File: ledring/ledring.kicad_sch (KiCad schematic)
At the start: 22 parts, among them U1 LM3914V, U2 LM3914V

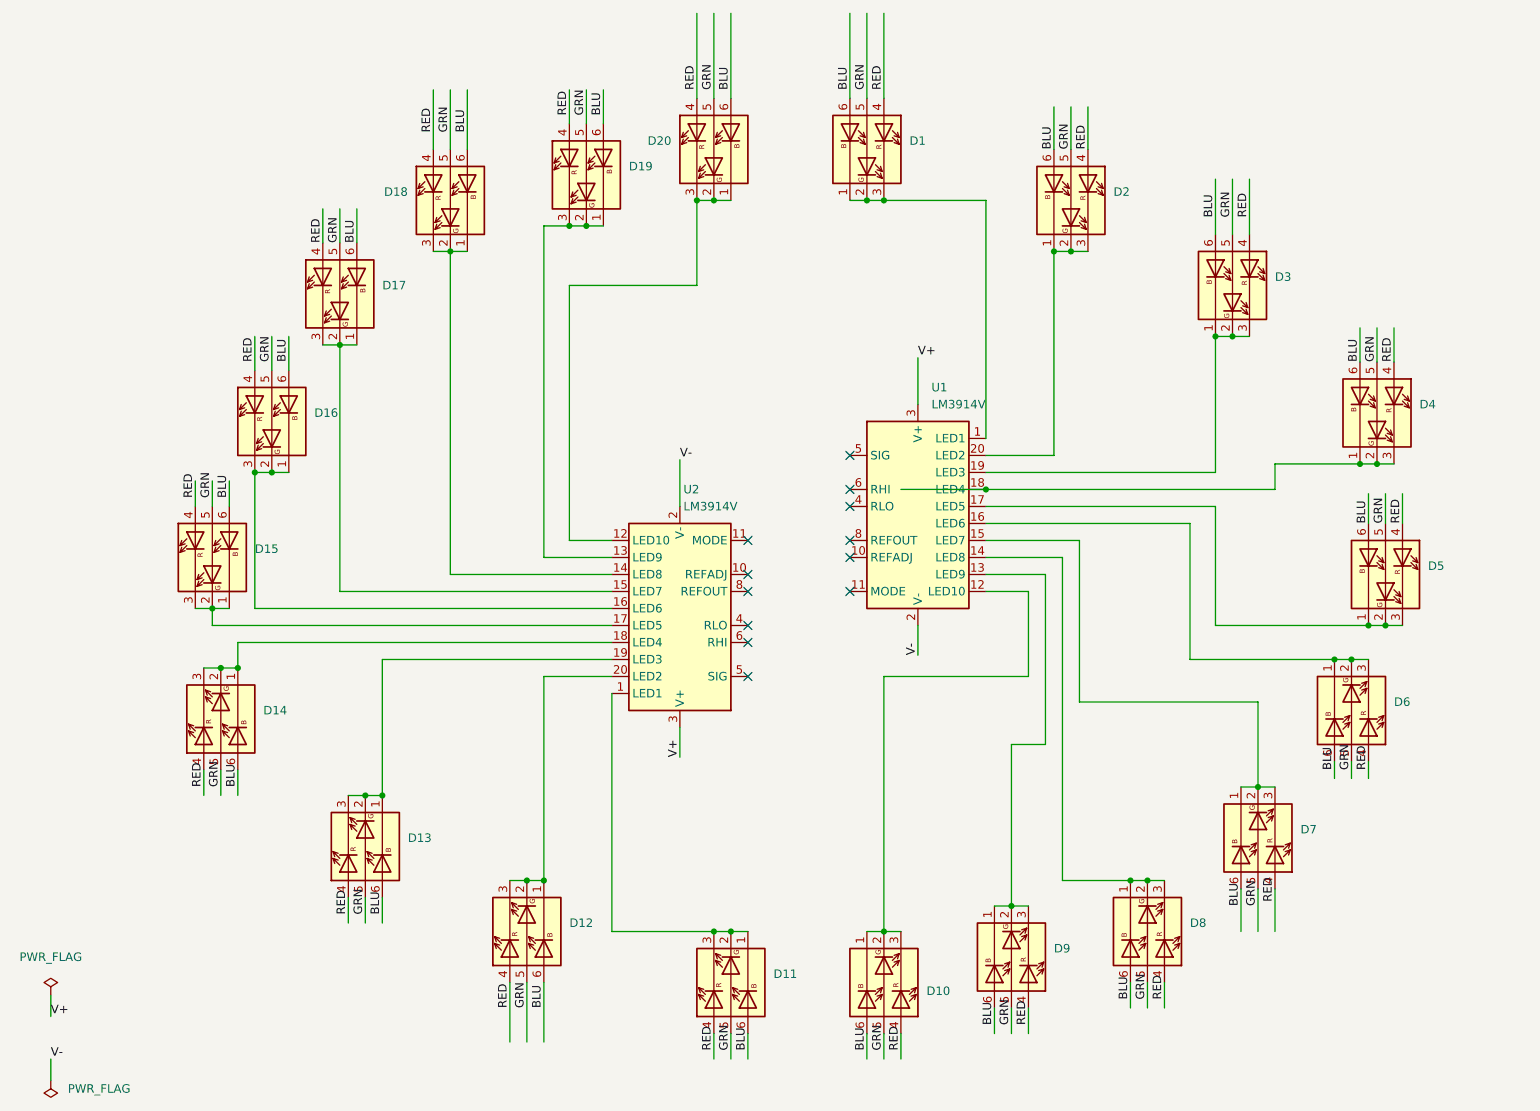
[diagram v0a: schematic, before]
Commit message: ledring: switch from LM3914V (PLCC-20) to LM3914N (DIP-18)
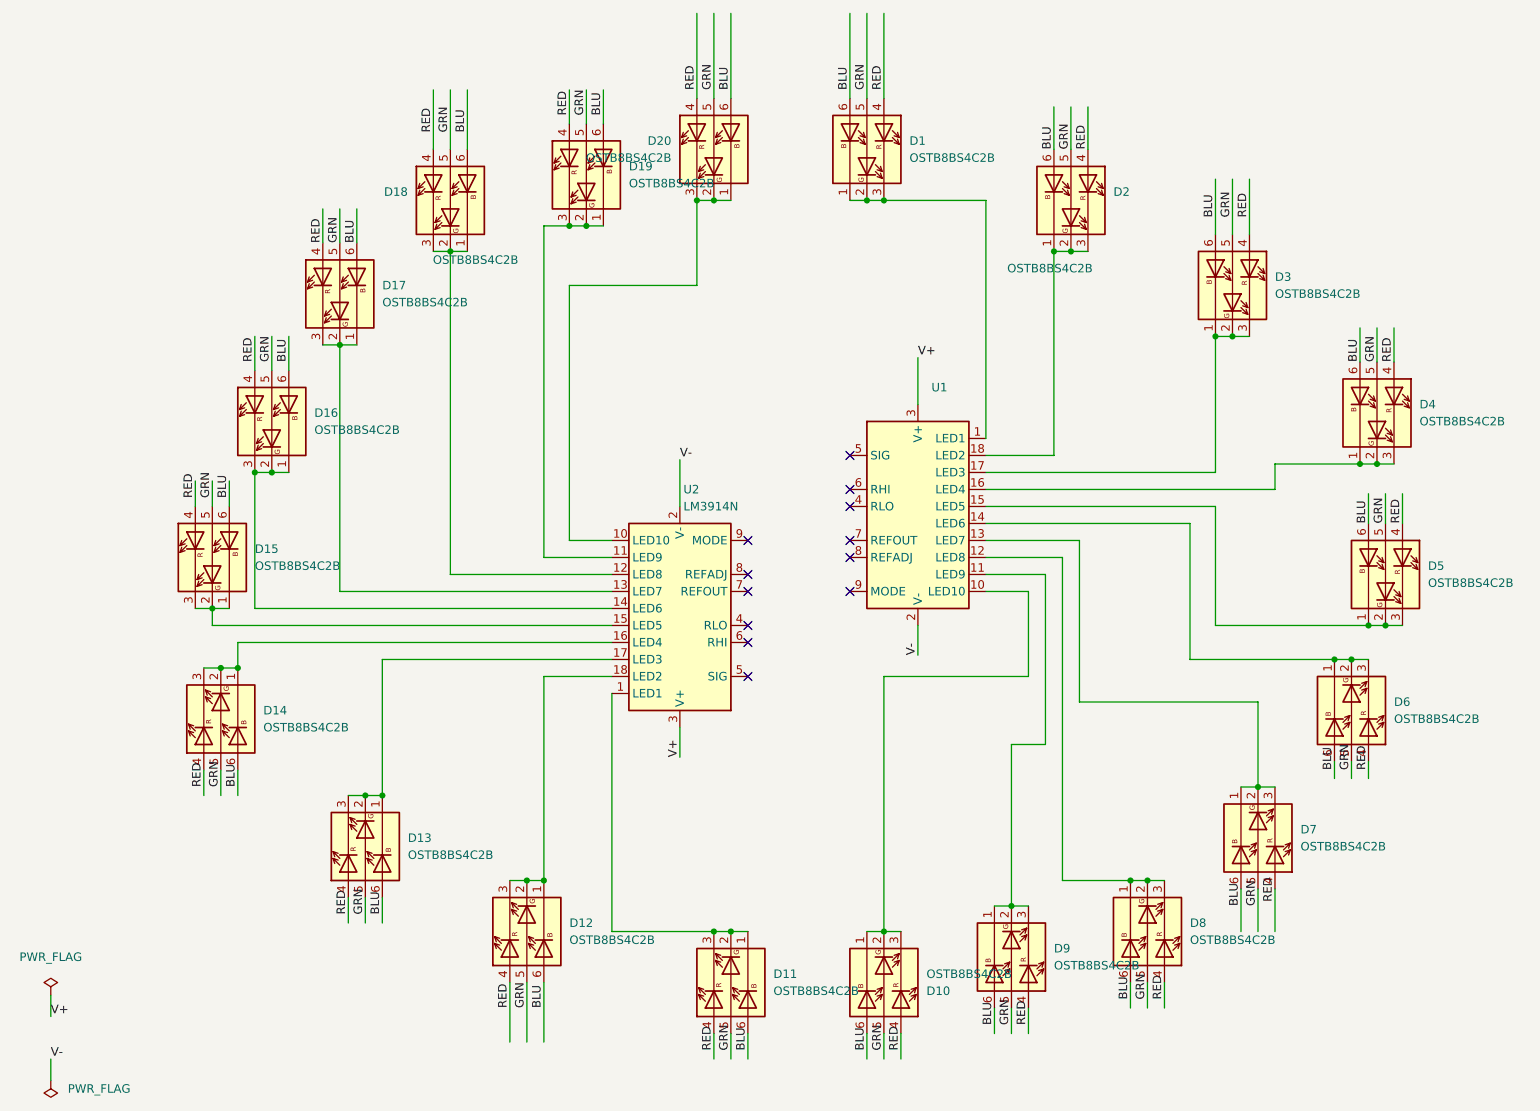
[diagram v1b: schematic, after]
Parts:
- removed U1, U2: LM3914V, Package_LCC:PLCC-20, symbol Driver_LED:LM3914V
- added U1: (no value), symbol nedko:LM3914N
- added U2: LM3914N, Package_DIP:DIP-18_W7.62mm_LongPads, symbol nedko:LM3914N
- D1: value (none) -> OSTB8BS4C2B; footprint (none) -> LED_SMD:LED_Avago_PLCC6_3x2.8mm
- D10, D11, D12, D13, D14, D15, D16, D17, D18, D19, D2, D20, D3, D4, D5, D6, D7, D8, D9: value (none) -> OSTB8BS4C2B
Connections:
- net V+: now also U1.3 (V+), U2.3 (V+)
- net V-: now also U1.2 (V-), U2.2 (V-)
- net at D2.1 (KB), D2.2 (KG), D2.3 (KR): now also U1.18 (LED2)
- net at D14.1 (KB), D14.2 (KG), D14.3 (KR): now also U2.16 (LED4)
- net at D16.1 (KB), D16.2 (KG), D16.3 (KR): now also U2.14 (LED6)
- net at D13.1 (KB), D13.2 (KG), D13.3 (KR): now also U2.17 (LED3)
- net at D3.1 (KB), D3.2 (KG), D3.3 (KR): now also U1.17 (LED3)
- net at D5.1 (KB), D5.2 (KG), D5.3 (KR): now also U1.15 (LED5)
- net at D9.1 (KB), D9.2 (KG), D9.3 (KR): now also U1.11 (LED9)
- net at D11.1 (KB), D11.2 (KG), D11.3 (KR): now also U2.1 (LED1)
- net at D6.1 (KB), D6.2 (KG), D6.3 (KR): now also U1.14 (LED6)
- net at D15.1 (KB), D15.2 (KG), D15.3 (KR): now also U2.15 (LED5)
- net at D12.1 (KB), D12.2 (KG), D12.3 (KR): now also U2.18 (LED2)
- net at D4.1 (KB), D4.2 (KG), D4.3 (KR): now also U1.16 (LED4)
- net at D19.1 (KB), D19.2 (KG), D19.3 (KR): now also U2.11 (LED9)
- net at D1.1 (KB), D1.2 (KG), D1.3 (KR): now also U1.1 (LED1)
- net at D17.1 (KB), D17.2 (KG), D17.3 (KR): now also U2.13 (LED7)
- net at D20.1 (KB), D20.2 (KG), D20.3 (KR): now also U2.10 (LED10)
- net at D18.1 (KB), D18.2 (KG), D18.3 (KR): now also U2.12 (LED8)
- net at D7.1 (KB), D7.2 (KG), D7.3 (KR): now also U1.13 (LED7)
- net at D10.1 (KB), D10.2 (KG), D10.3 (KR): now also U1.10 (LED10)
- net at D8.1 (KB), D8.2 (KG), D8.3 (KR): now also U1.12 (LED8)
